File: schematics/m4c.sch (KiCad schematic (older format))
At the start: 21 parts

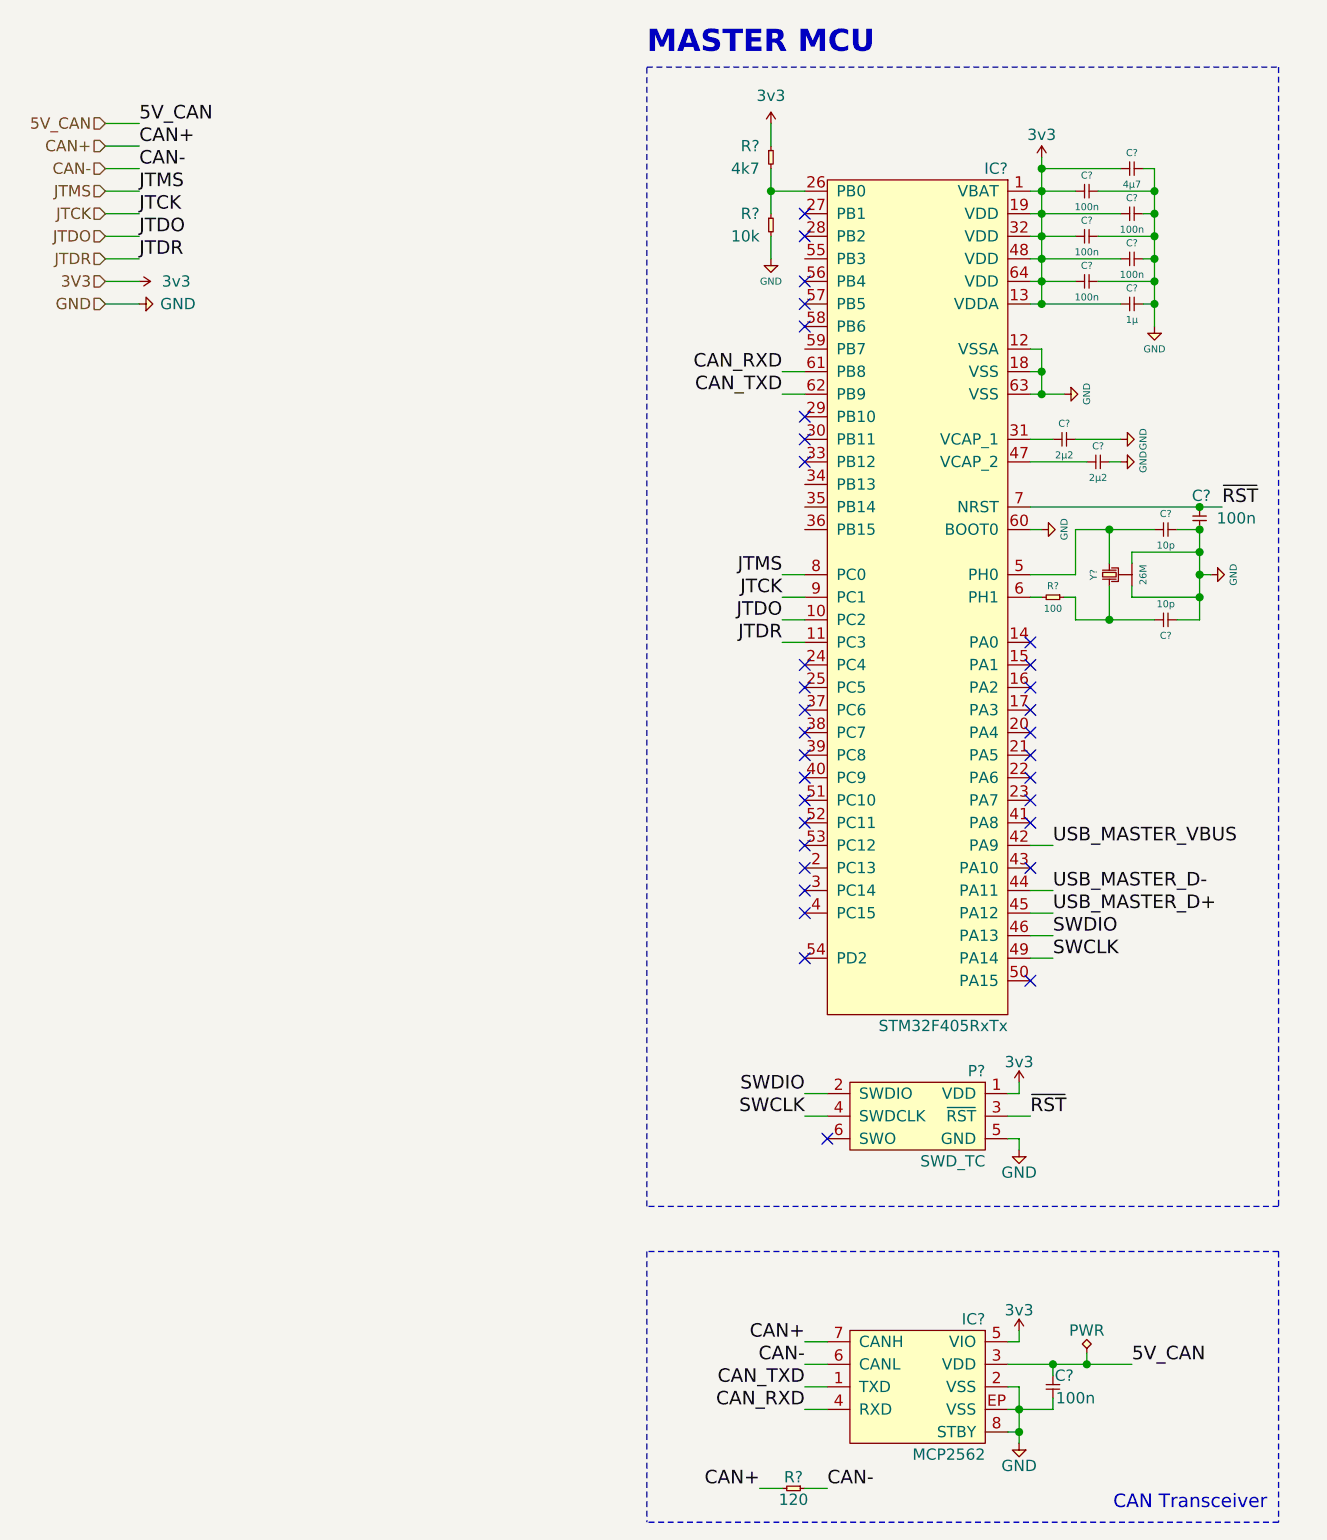
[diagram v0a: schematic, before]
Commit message: Restructure main schematic bus layout
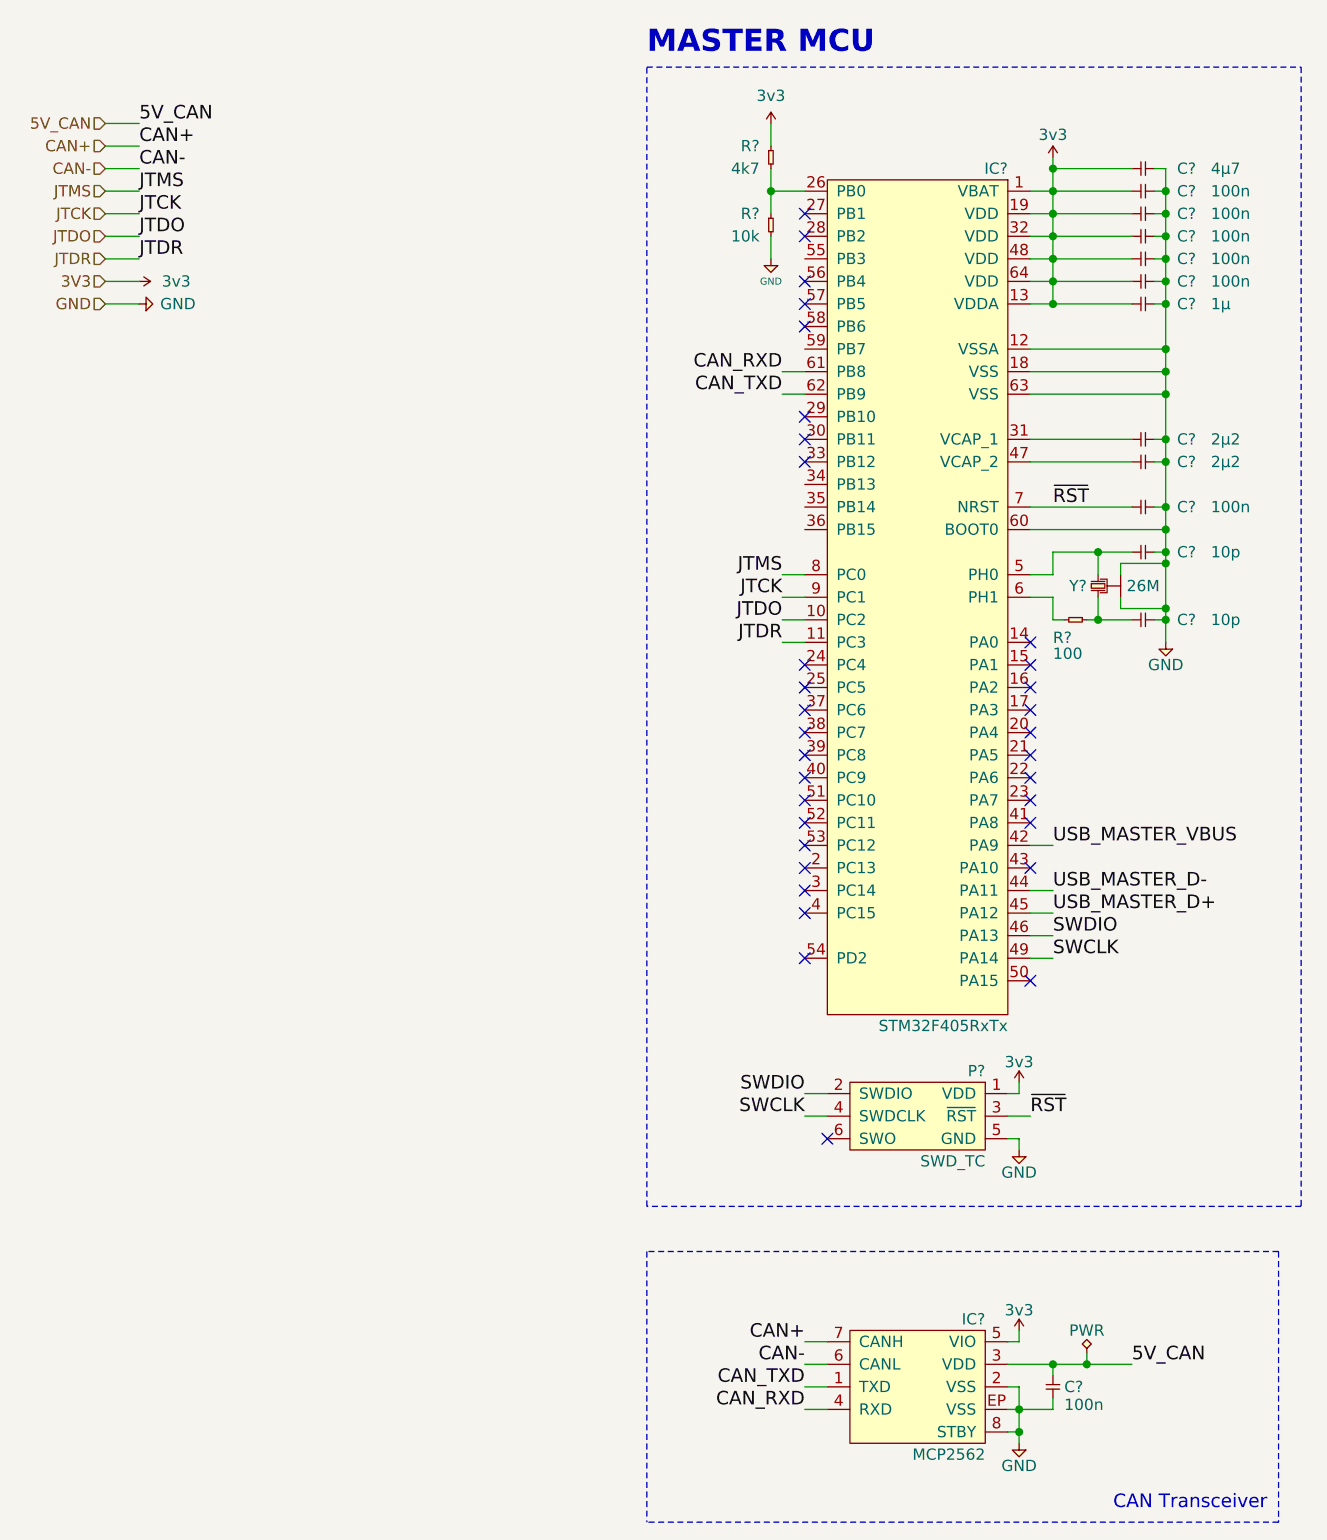
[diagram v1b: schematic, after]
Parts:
- removed C?: 100n, symbol cusf-kicad:C
- removed C? (x6): 100n, agg:0402, symbol cusf-kicad:C
- removed C?: 2µ2, agg:0402, symbol cusf-kicad:C
- removed C? (x2): 10p, agg:0402, symbol cusf-kicad:C
- removed R?: 120, agg:0603, symbol cusf-kicad:R
- added C? (x7): 100n, agg:0402, symbol cusf-kicad:C
- added C?: 2µ2, agg:0402, symbol cusf-kicad:C
- added C? (x2): 10p, agg:0402, symbol cusf-kicad:C
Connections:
- net 3v3: now also C?.2, C?.2, C?.2, C?.2, C?.2
- net 5V_CAN: now also C?.1
- net GND: now also C?.1, C?.1, C?.1, C?.1, C?.1, C?.1, C?.1, C?.1, C?.1, C?.1, C?.2; no longer C?.2
- net ~RST: now also C?.2
- net at IC?.47 (VCAP_2): now also C?.2
- net at IC?.31 (VCAP_1): now also C?.2; no longer C?.1
- net at R?.1, Y?.3: now also C?.2
- net at IC?.5 (PH0), Y?.1: now also C?.2
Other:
- moved on the sheet: C?, R?, Y?

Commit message: Normalise all font sizes to 50 mil
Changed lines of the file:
@@
 Comment2 ""
 Comment3 ""
-Comment4 "Drawn by: Henry Franks"
+Comment4 "Drawn by Henry Franks"
 $EndDescr
 $Comp
@@
 NoConn ~ 5350 3750
 NoConn ~ 5350 3650
-Text Label 5450 2850 0    60   ~ 0
+Text Label 5450 2850 0    50   ~ 0
 ~RST
 NoConn ~ 4350 4850
@@
 NoConn ~ 4350 4050
 NoConn ~ 4350 3950
-Text Label 4250 3450 2    60   ~ 0
+Text Label 4250 3450 2    50   ~ 0
 JTDR
-Text Label 5450 4850 0    60   ~ 0
+Text Label 5450 4850 0    50   ~ 0
 SWCLK
-Text Label 5450 4750 0    60   ~ 0
+Text Label 5450 4750 0    50   ~ 0
 SWDIO
-Text Label 4350 5550 2    60   ~ 0
+Text Label 4350 5550 2    50   ~ 0
 SWCLK
-Text Label 4350 5450 2    60   ~ 0
+Text Label 4350 5450 2    50   ~ 0
 SWDIO
 Wire Wire Line
@@
 L cusf-kicad:GND #PWR?
 U 1 1 605FBAC1
-P 5950 3450
+P 5950 3400
 AR Path="/6013AE2F/605FBAC1" Ref="#PWR?"  Part="1"
 AR Path="/605FBAC1" Ref="#PWR?"  Part="1"
 AR Path="/605DF50F/605FBAC1" Ref="#PWR?"  Part="1"
-F 0 "#PWR?" H 5820 3490 50  0001 L CNN
-F 1 "GND" H 5950 3350 50  0000 C CNN
-F 2 "" H 5950 3450 60  0000 C CNN
-F 3 "" H 5950 3450 60  0000 C CNN
-	1    5950 3450
+F 0 "#PWR?" H 5820 3440 50  0001 L CNN
+F 1 "GND" H 5950 3300 50  0000 C CNN
+F 2 "" H 5950 3400 50  0000 C CNN
+F 3 "" H 5950 3400 50  0000 C CNN
+	1    5950 3400
 	-1   0    0    -1
 $EndComp
@@
 F 2 "agg:XTAL-20x16" H 5700 2930 50  0001 C CNN
 F 3 "" H 5650 3150 50  0001 C CNN
-F 4 "2506952" H 5650 3150 60  0001 C CNN "Farnell"
+F 4 "2506952" H 5650 3150 50  0001 C CNN "Farnell"
 	1    5650 3150
 	0    -1   1    0
@@
 F 0 "#PWR?" H 5300 5510 50  0001 L CNN
 F 1 "3v3" H 5300 5490 50  0000 C CNN
-F 2 "" H 5300 5400 60  0000 C CNN
-F 3 "" H 5300 5400 60  0000 C CNN
+F 2 "" H 5300 5400 50  0000 C CNN
+F 3 "" H 5300 5400 50  0000 C CNN
 	1    5300 5400
 	-1   0    0    -1
 $EndComp
-Text Label 5350 5550 0    60   ~ 0
+Text Label 5350 5550 0    50   ~ 0
 ~RST
 NoConn ~ 4450 5650
@@
 	-1   0    0    -1
 $EndComp
-Text Label 5450 4550 0    60   ~ 0
+Text Label 5450 4550 0    50   ~ 0
 USB_MASTER_D-
-Text Label 5450 4650 0    60   ~ 0
+Text Label 5450 4650 0    50   ~ 0
 USB_MASTER_D+
-Text Label 5450 4350 0    60   ~ 0
+Text Label 5450 4350 0    50   ~ 0
 USB_MASTER_VBUS
-Text Label 4250 3150 2    60   ~ 0
+Text Label 4250 3150 2    50   ~ 0
 JTMS
-Text Label 4250 3250 2    60   ~ 0
+Text Label 4250 3250 2    50   ~ 0
 JTCK
-Text Label 4250 2250 2    60   ~ 0
+Text Label 4250 2250 2    50   ~ 0
 CAN_RXD
-Text Label 4250 2350 2    60   ~ 0
+Text Label 4250 2350 2    50   ~ 0
 CAN_TXD
 NoConn ~ 4350 4650
@@
 NoConn ~ 4350 2450
 NoConn ~ 4350 1650
-Text Label 4250 3350 2    60   ~ 0
+Text Label 4250 3350 2    50   ~ 0
 JTDO
 NoConn ~ 4350 1550
@@
 	-1   0    0    -1
 $EndComp
-Text Label 4350 6550 2    60   ~ 0
+Text Label 4350 6550 2    50   ~ 0
 CAN+
 $Comp
@@
 F 0 "#PWR?" H 5300 6610 50  0001 L CNN
 F 1 "3v3" H 5300 6590 50  0000 C CNN
-F 2 "" H 5300 6500 60  0000 C CNN
-F 3 "" H 5300 6500 60  0000 C CNN
+F 2 "" H 5300 6500 50  0000 C CNN
+F 3 "" H 5300 6500 50  0000 C CNN
 	1    5300 6500
 	-1   0    0    -1
@@
 F 0 "#PWR?" H 5170 7040 50  0001 L CNN
 F 1 "GND" H 5300 6900 50  0000 C CNN
-F 2 "" H 5300 7000 60  0000 C CNN
-F 3 "" H 5300 7000 60  0000 C CNN
+F 2 "" H 5300 7000 50  0000 C CNN
+F 3 "" H 5300 7000 50  0000 C CNN
 	1    5300 7000
 	-1   0    0    -1
 $EndComp
-Text Label 4350 6650 2    60   ~ 0
+Text Label 4350 6650 2    50   ~ 0
 CAN-
-Text Label 4350 6750 2    60   ~ 0
+Text Label 4350 6750 2    50   ~ 0
 CAN_TXD
-Text Label 4350 6850 2    60   ~ 0
+Text Label 4350 6850 2    50   ~ 0
 CAN_RXD
 Wire Wire Line
@@
 	5250 6950 5300 6950
 Connection ~ 5300 6950
-Text Notes 6400 7300 2    60   ~ 0
+Text Notes 6400 7300 2    50   ~ 0
 CAN Transceiver
 Wire Wire Line
@@
 Wire Notes Line
 	6450 7350 3650 7350
-Text Label 5800 6650 0    60   ~ 0
+Text Label 5800 6650 0    50   ~ 0
 5V_CAN
 Wire Notes Line
@@
 Text Notes 3650 850  0    98   ~ 20
 MASTER MCU
-Text Label 1400 1450 0    60   ~ 0
+Text Label 1400 1450 0    50   ~ 0
 JTMS
-Text Label 1400 1550 0    60   ~ 0
+Text Label 1400 1550 0    50   ~ 0
 JTCK
-Text Label 1400 1150 0    60   ~ 0
+Text Label 1400 1150 0    50   ~ 0
 5V_CAN
-Text Label 1400 1350 0    60   ~ 0
+Text Label 1400 1350 0    50   ~ 0
 CAN-
-Text Label 1400 1250 0    60   ~ 0
+Text Label 1400 1250 0    50   ~ 0
 CAN+
-Text Label 1400 1650 0    60   ~ 0
+Text Label 1400 1650 0    50   ~ 0
 JTDO
 Wire Wire Line
@@
 Wire Wire Line
 	4350 3150 4250 3150
-Text Label 1400 1750 0    60   ~ 0
+Text Label 1400 1750 0    50   ~ 0
 JTDR
 Wire Wire Line
@@
 F 2 "agg:0402" H 5900 2550 50  0001 C CNN
 F 3 "" H 5900 2550 50  0001 C CNN
-F 4 "2362088" H 5900 2550 60  0001 C CNN "Farnell"
+F 4 "2362088" H 5900 2550 50  0001 C CNN "Farnell"
 	1    5900 2550
 	-1   0    0    1
@@
 F 2 "agg:0402" H 5900 2650 50  0001 C CNN
 F 3 "" H 5900 2650 50  0001 C CNN
-F 4 "2362088" H 5900 2650 60  0001 C CNN "Farnell"
+F 4 "2362088" H 5900 2650 50  0001 C CNN "Farnell"
 	1    5900 2650
 	-1   0    0    1
@@
 F 2 "agg:0402" H 5900 1450 50  0001 C CNN
 F 3 "" H 5900 1450 50  0001 C CNN
-F 4 "2496771" H 5900 1450 60  0001 C CNN "Farnell"
+F 4 "2496771" H 5900 1450 50  0001 C CNN "Farnell"
 	1    5900 1450
 	-1   0    0    -1
@@
 F 2 "agg:0402" H 5900 1850 50  0001 C CNN
 F 3 "" H 5900 1850 50  0001 C CNN
-F 4 "2496771" H 5900 1850 60  0001 C CNN "Farnell"
+F 4 "2496771" H 5900 1850 50  0001 C CNN "Farnell"
 	1    5900 1850
 	-1   0    0    -1
@@
 F 2 "agg:0402" H 5900 1750 50  0001 C CNN
 F 3 "" H 5900 1750 50  0001 C CNN
-F 4 "2496771" H 5900 1750 60  0001 C CNN "Farnell"
+F 4 "2496771" H 5900 1750 50  0001 C CNN "Farnell"
 	1    5900 1750
 	-1   0    0    -1
@@
 F 2 "agg:0402" H 5900 1650 50  0001 C CNN
 F 3 "" H 5900 1650 50  0001 C CNN
-F 4 "2496771" H 5900 1650 60  0001 C CNN "Farnell"
+F 4 "2496771" H 5900 1650 50  0001 C CNN "Farnell"
 	1    5900 1650
 	-1   0    0    -1
@@
 F 2 "agg:0402" H 5900 1550 50  0001 C CNN
 F 3 "" H 5900 1550 50  0001 C CNN
-F 4 "2496771" H 5900 1550 60  0001 C CNN "Farnell"
+F 4 "2496771" H 5900 1550 50  0001 C CNN "Farnell"
 	1    5900 1550
 	-1   0    0    -1
@@
 F 2 "agg:0402" H 5900 1950 50  0001 C CNN
 F 3 "" H 5900 1950 50  0001 C CNN
-F 4 "2496814" H 5900 1950 60  0001 C CNN "Farnell"
+F 4 "2496814" H 5900 1950 50  0001 C CNN "Farnell"
 	1    5900 1950
 	-1   0    0    -1
@@
 F 2 "agg:0402" H 5900 1350 50  0001 C CNN
 F 3 "" H 5900 1350 50  0001 C CNN
-F 4 "2426952" H 5900 1350 60  0001 C CNN "Farnell"
+F 4 "2426952" H 5900 1350 50  0001 C CNN "Farnell"
 	1    5900 1350
 	-1   0    0    -1
@@
 F 2 "agg:0402" H 5900 2850 50  0001 C CNN
 F 3 "" H 5900 2850 50  0001 C CNN
-F 4 "2496771" H 5900 2850 60  0001 C CNN "Farnell"
+F 4 "2496771" H 5900 2850 50  0001 C CNN "Farnell"
 	1    5900 2850
 	-1   0    0    -1
@@
 F 2 "agg:0402" H 5900 3050 50  0001 C CNN
 F 3 "" H 5900 3050 50  0001 C CNN
-F 4 "2496771" H 5900 3050 60  0001 C CNN "Farnell"
+F 4 "2496771" H 5900 3050 50  0001 C CNN "Farnell"
 	1    5900 3050
 	-1   0    0    -1
@@
 F 2 "agg:0402" H 5900 3350 50  0001 C CNN
 F 3 "" H 5900 3350 50  0001 C CNN
-F 4 "2496771" H 5900 3350 60  0001 C CNN "Farnell"
+F 4 "2496771" H 5900 3350 50  0001 C CNN "Farnell"
 	1    5900 3350
 	-1   0    0    -1
@@
 Connection ~ 5950 3350
 Wire Wire Line
-	5950 3350 5950 3450
+	5950 3350 5950 3400
 Wire Wire Line
 	5950 3300 5950 3350
@@
 F 2 "agg:0402" H 5600 3350 50  0001 C CNN
 F 3 "" H 5600 3350 50  0001 C CNN
-F 4 "9239111" H 5600 3350 60  0001 C CNN "Farnell"
+F 4 "9239111" H 5600 3350 50  0001 C CNN "Farnell"
 	1    5600 3350
 	-1   0    0    -1
@@
 F 2 "agg:0402" H 5450 6700 50  0001 C CNN
 F 3 "" H 5450 6700 50  0001 C CNN
-F 4 "2496771" H 5450 6700 60  0001 C CNN "Farnell"
+F 4 "2496771" H 5450 6700 50  0001 C CNN "Farnell"
 	1    5450 6700
 	0    -1   1    0
